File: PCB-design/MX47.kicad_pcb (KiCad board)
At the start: 2 copper layers, 238.8 x 86.4 mm, 124 parts, among them J1 Conn_01x12, J2 Conn_01x12, U1 CherryMX_LTST-A683CEGBW, U10 CherryMX_LTST-A683CEGBW, U11 CherryMX_LTST-A683CEGBW, U12 CherryMX_LTST-A683CEGBW, U13 CherryMX_LTST-A683CEGBW, U14 CherryMX_LTST-A683CEGBW, U15 CherryMX_LTST-A683CEGBW, U16 CherryMX_LTST-A683CEGBW, U17 CherryMX_LTST-A683CEGBW, U18 CherryMX_LTST-A683CEGBW, U19 CherryMX_LTST-A683CEGBW, U2 CherryMX_LTST-A683CEGBW, U20 CherryMX_LTST-A683CEGBW, U21 CherryMX_LTST-A683CEGBW, U22 CherryMX_LTST-A683CEGBW, U23 CherryMX_LTST-A683CEGBW, U24 CherryMX_LTST-A683CEGBW, U25 CherryMX_LTST-A683CEGBW, U26 CherryMX_LTST-A683CEGBW, U27 CherryMX_LTST-A683CEGBW, U28 CherryMX_LTST-A683CEGBW, U29 CherryMX_LTST-A683CEGBW, U3 CherryMX_LTST-A683CEGBW, U30 CherryMX_LTST-A683CEGBW, U31 CherryMX_LTST-A683CEGBW, U32 CherryMX_LTST-A683CEGBW, U33 CherryMX_LTST-A683CEGBW, U34 CherryMX_LTST-A683CEGBW, U35 CherryMX_LTST-A683CEGBW, U36 CherryMX_LTST-A683CEGBW, U37 CherryMX_LTST-A683CEGBW, U38 CherryMX_LTST-A683CEGBW, U39 CherryMX_LTST-A683CEGBW, U4 CherryMX_LTST-A683CEGBW, U40 CherryMX_LTST-A683CEGBW, U41 CherryMX_LTST-A683CEGBW, U42 CherryMX_LTST-A683CEGBW, U43 CherryMX_LTST-A683CEGBW, U44 CherryMX_LTST-A683CEGBW, U45 CherryMX_LTST-A683CEGBW, U46 CherryMX_LTST-A683CEGBW, U47 CherryMX_LTST-A683CEGBW, U5 CherryMX_LTST-A683CEGBW, U6 CherryMX_LTST-A683CEGBW, U7 CherryMX_LTST-A683CEGBW, U8 CherryMX_LTST-A683CEGBW, U9 CherryMX_LTST-A683CEGBW

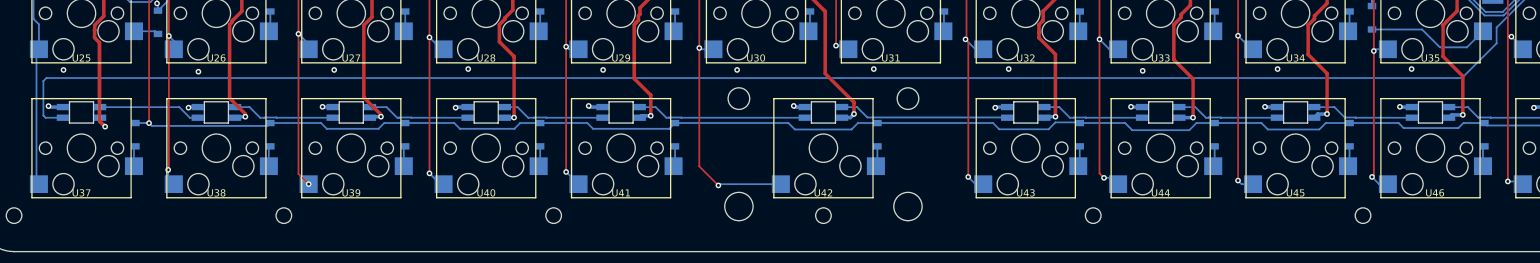
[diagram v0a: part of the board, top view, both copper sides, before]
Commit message: fix spacebar footprint
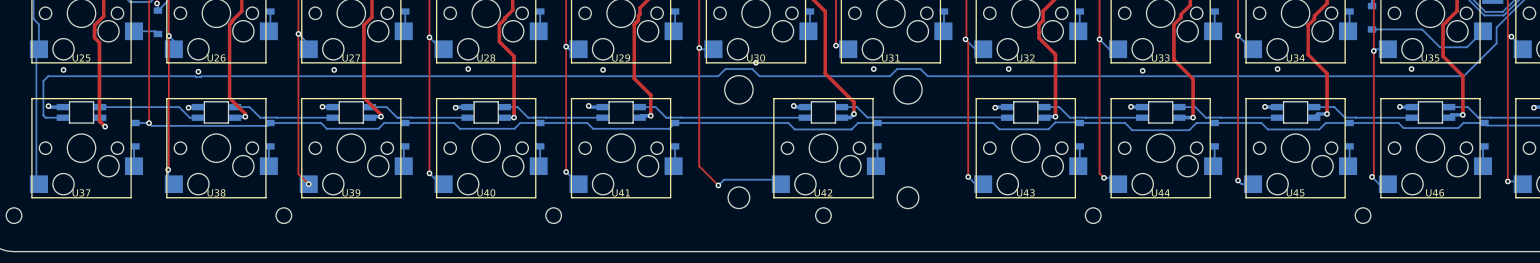
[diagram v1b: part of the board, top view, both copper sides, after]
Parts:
- U42: footprint CherryMX_KailhSocket_StabWireTop_LTST-A683CEGBW-Rotated:CherryMX_2.00u_KailhSocket_StabWireTop_LTST-A683CEGBW-Rotated -> CherryMX_PCB_KailhSocket_StabWireBottom_LTST-A683CEGBW-Rotated:CherryMX_2.00u_PCB_KailhSocket_StabWireBottom_LTST-A683C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
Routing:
- net Net-(U36-Pad5): track 239.0 -> 240.7 mm
- net COL6: track 187.8 -> 188.3 mm

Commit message: minor updates
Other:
- board text added: "License: CERN-OHL-W https://github.com/jpconstantineau/GridMX47 2021-09-28"
- board text removed: "License: CERN-OHL-W https://github.com/jpconstantineau/GridMX47 2021-08-30"
